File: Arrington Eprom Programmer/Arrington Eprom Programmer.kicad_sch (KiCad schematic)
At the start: 12 parts, among them J1 PGM volt in, J2 DB25_Male, SW1 SW_SPDT, U1 74LS164, U2 2716, U3 74LS299, U4 4N35

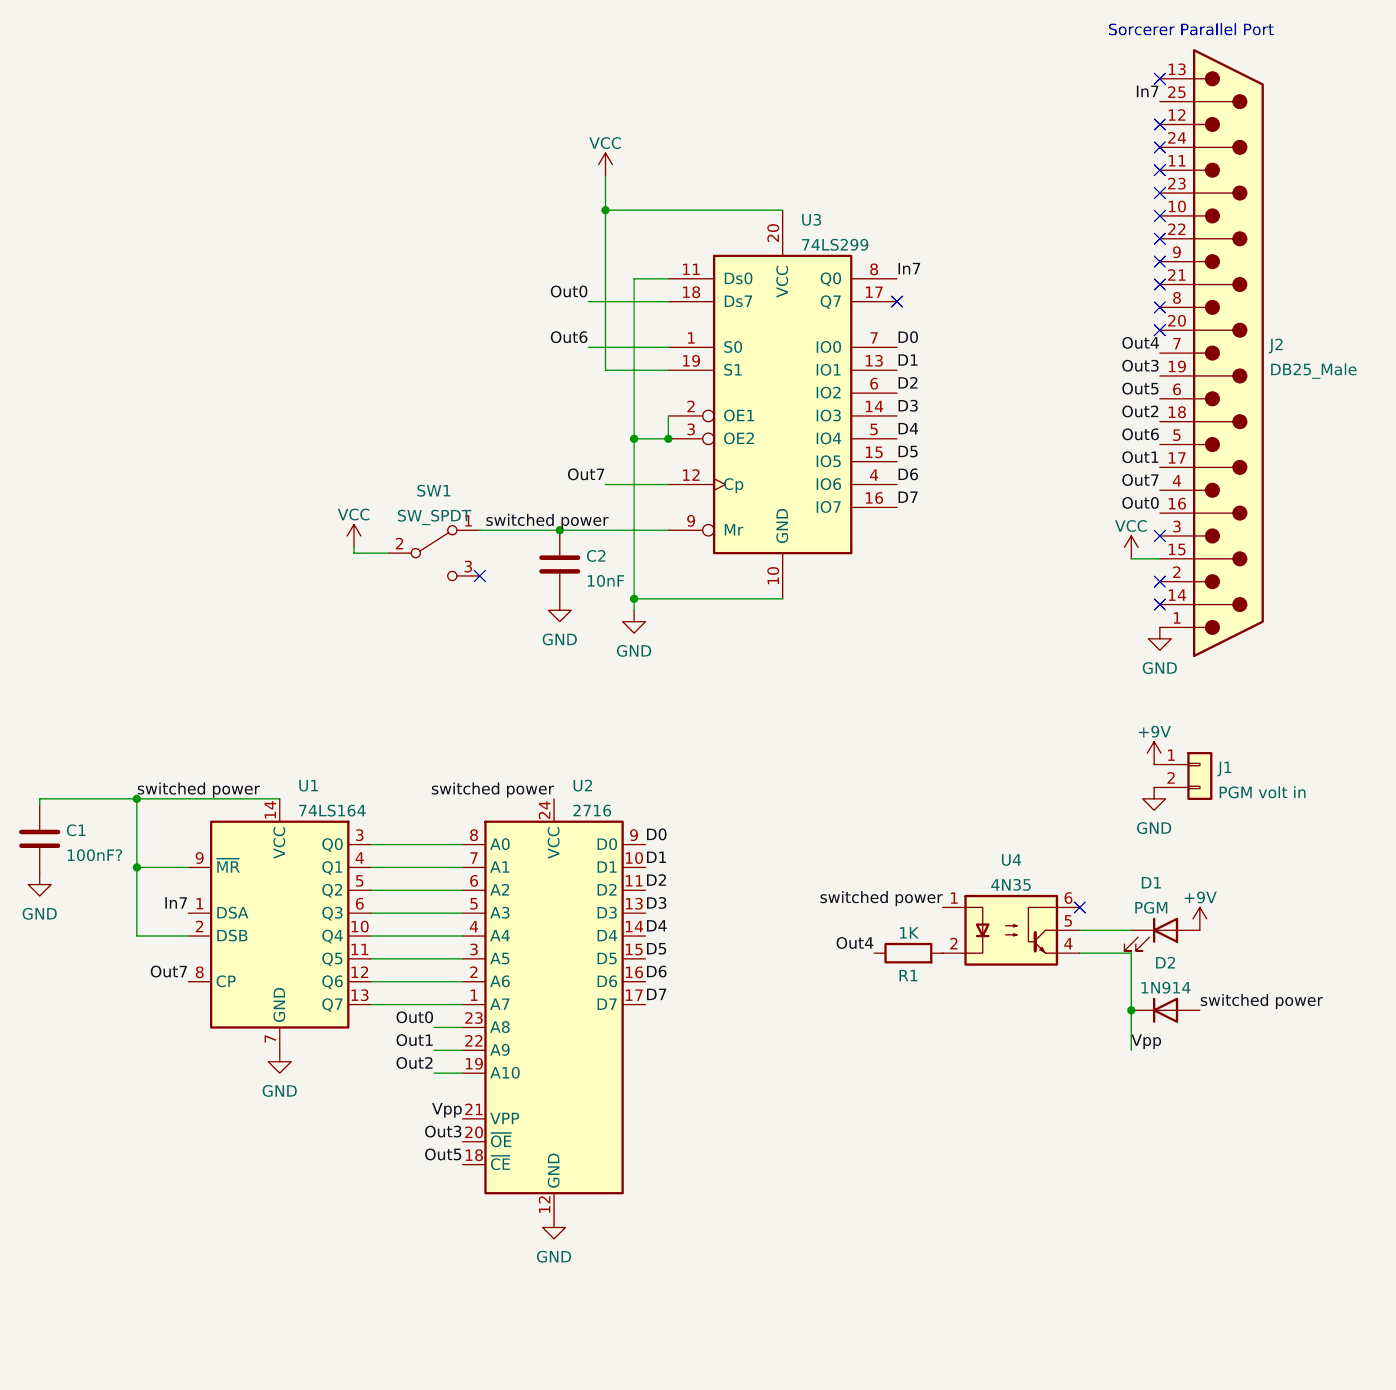
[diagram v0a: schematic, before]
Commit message: updates to be closer to real one
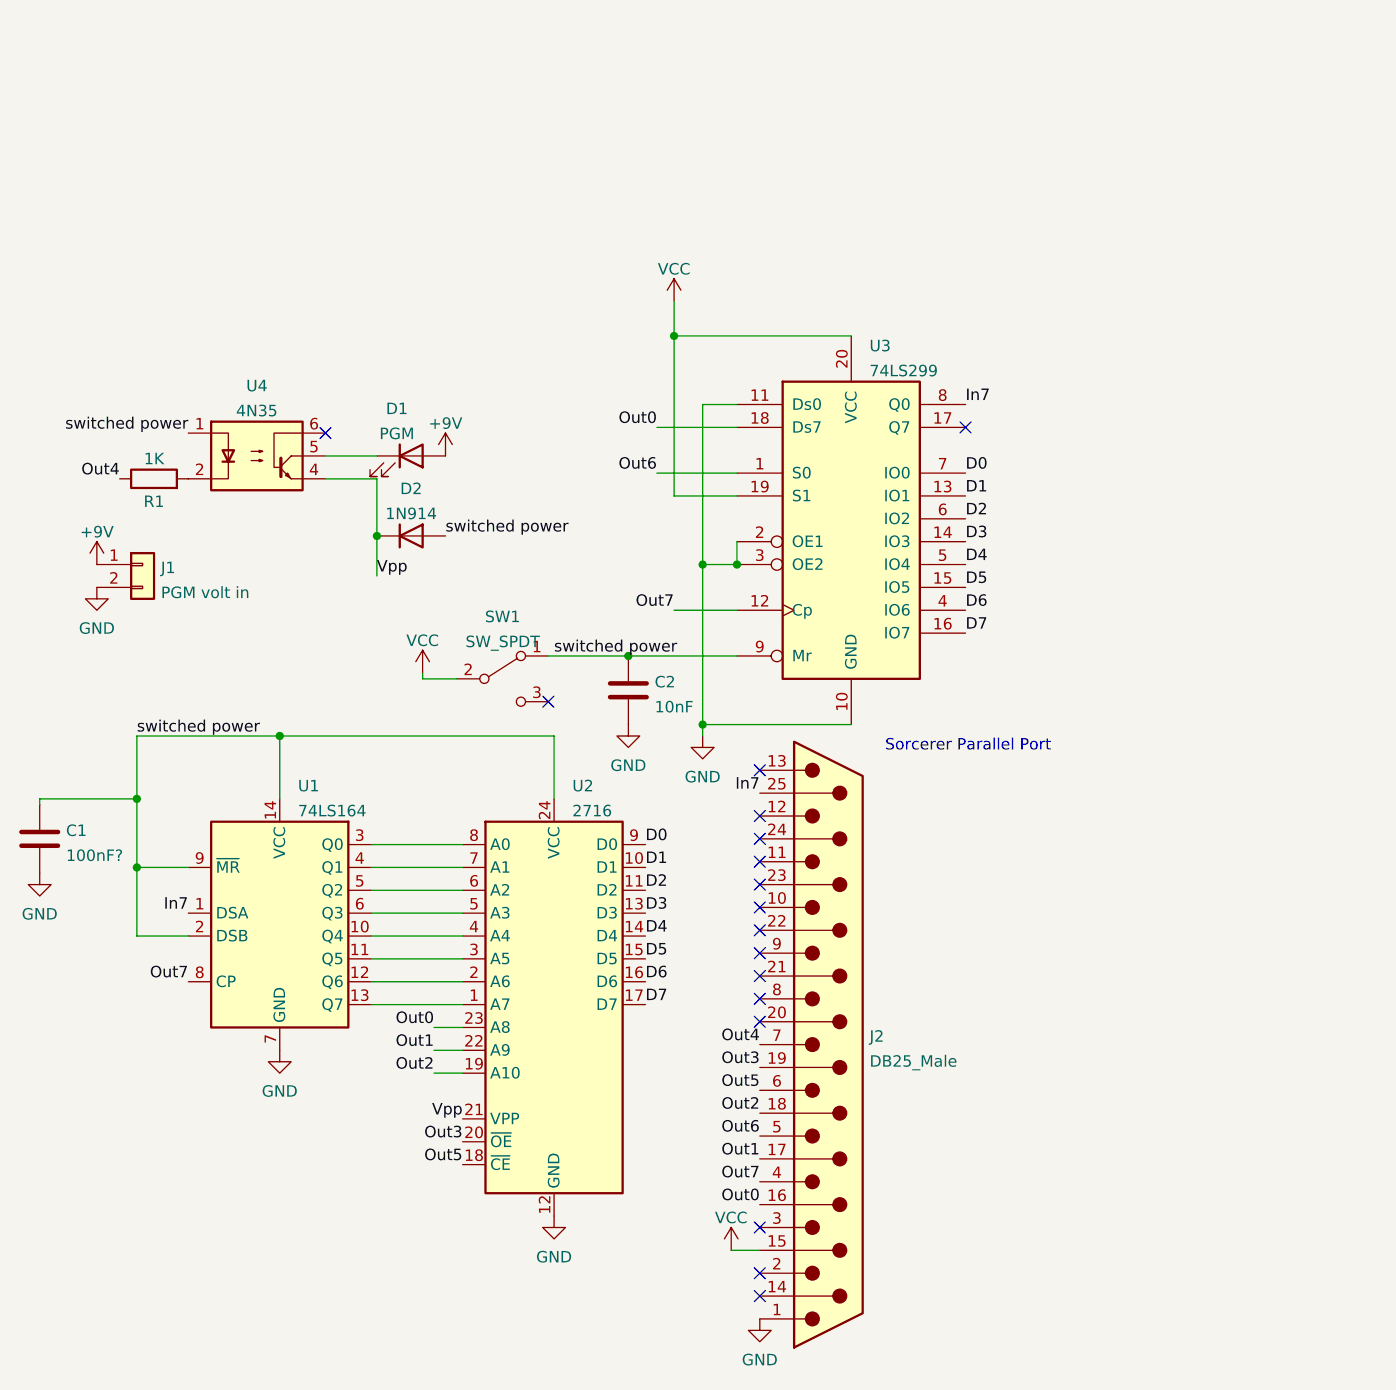
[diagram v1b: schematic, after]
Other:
- moved on the sheet: C2, D1, D2, J1, J2, R1, SW1, U3, U4
